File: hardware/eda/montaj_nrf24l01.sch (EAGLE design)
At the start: 4 parts, among them X1 MINI-USB-SHIELD-UX60-MB-5S8

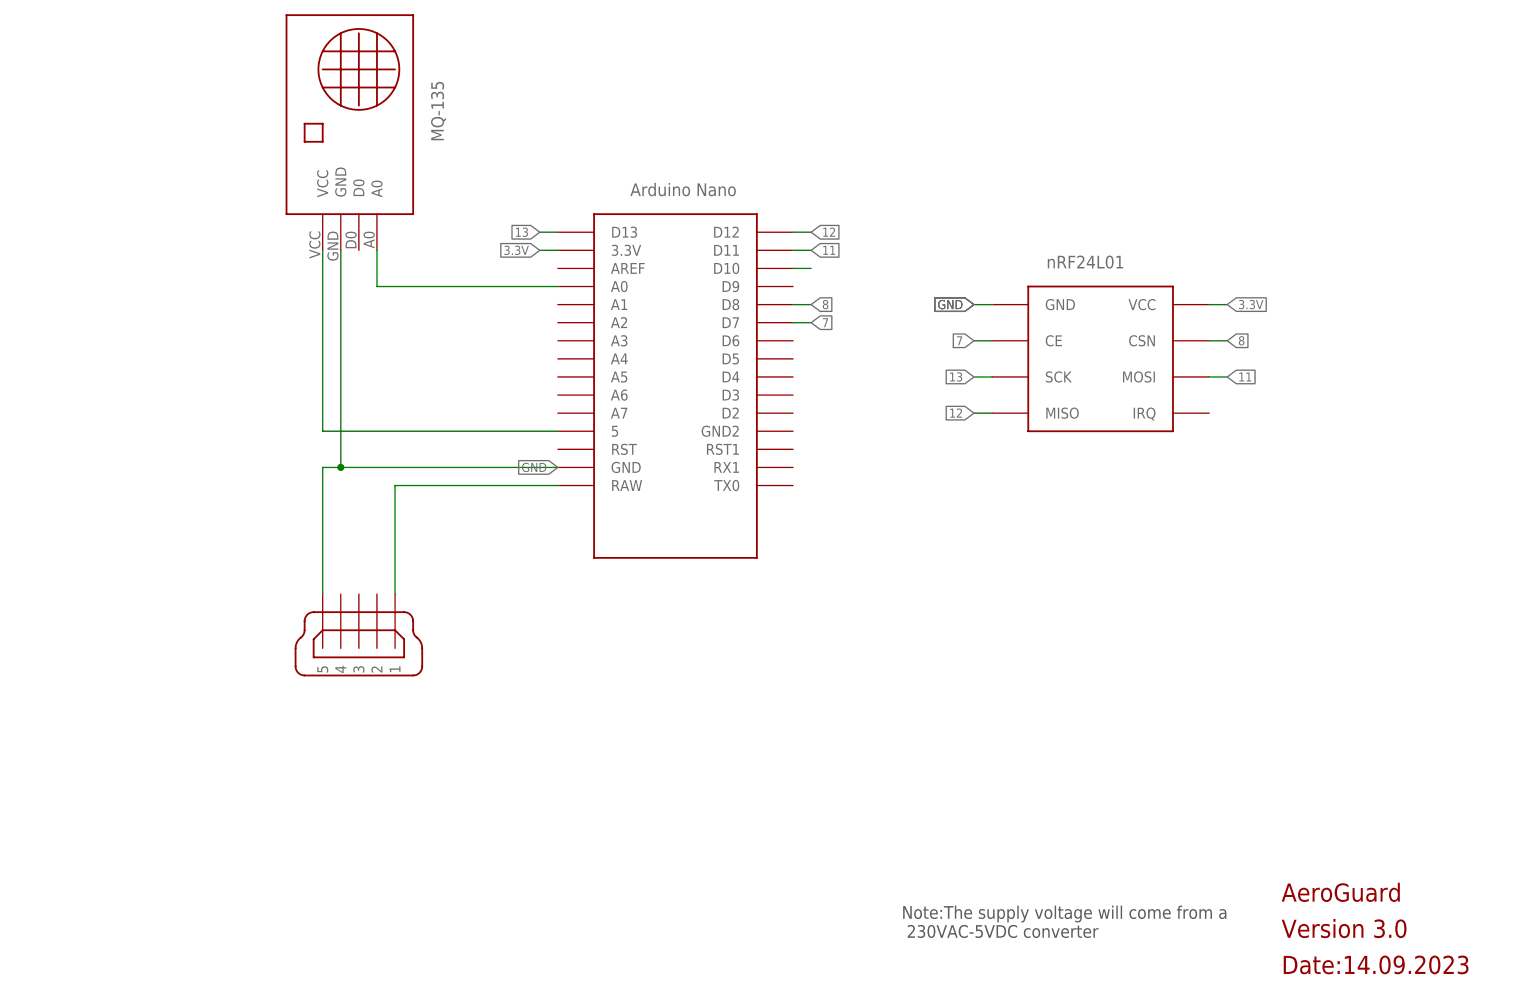
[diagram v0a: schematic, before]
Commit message: Adaugare modul DHT11
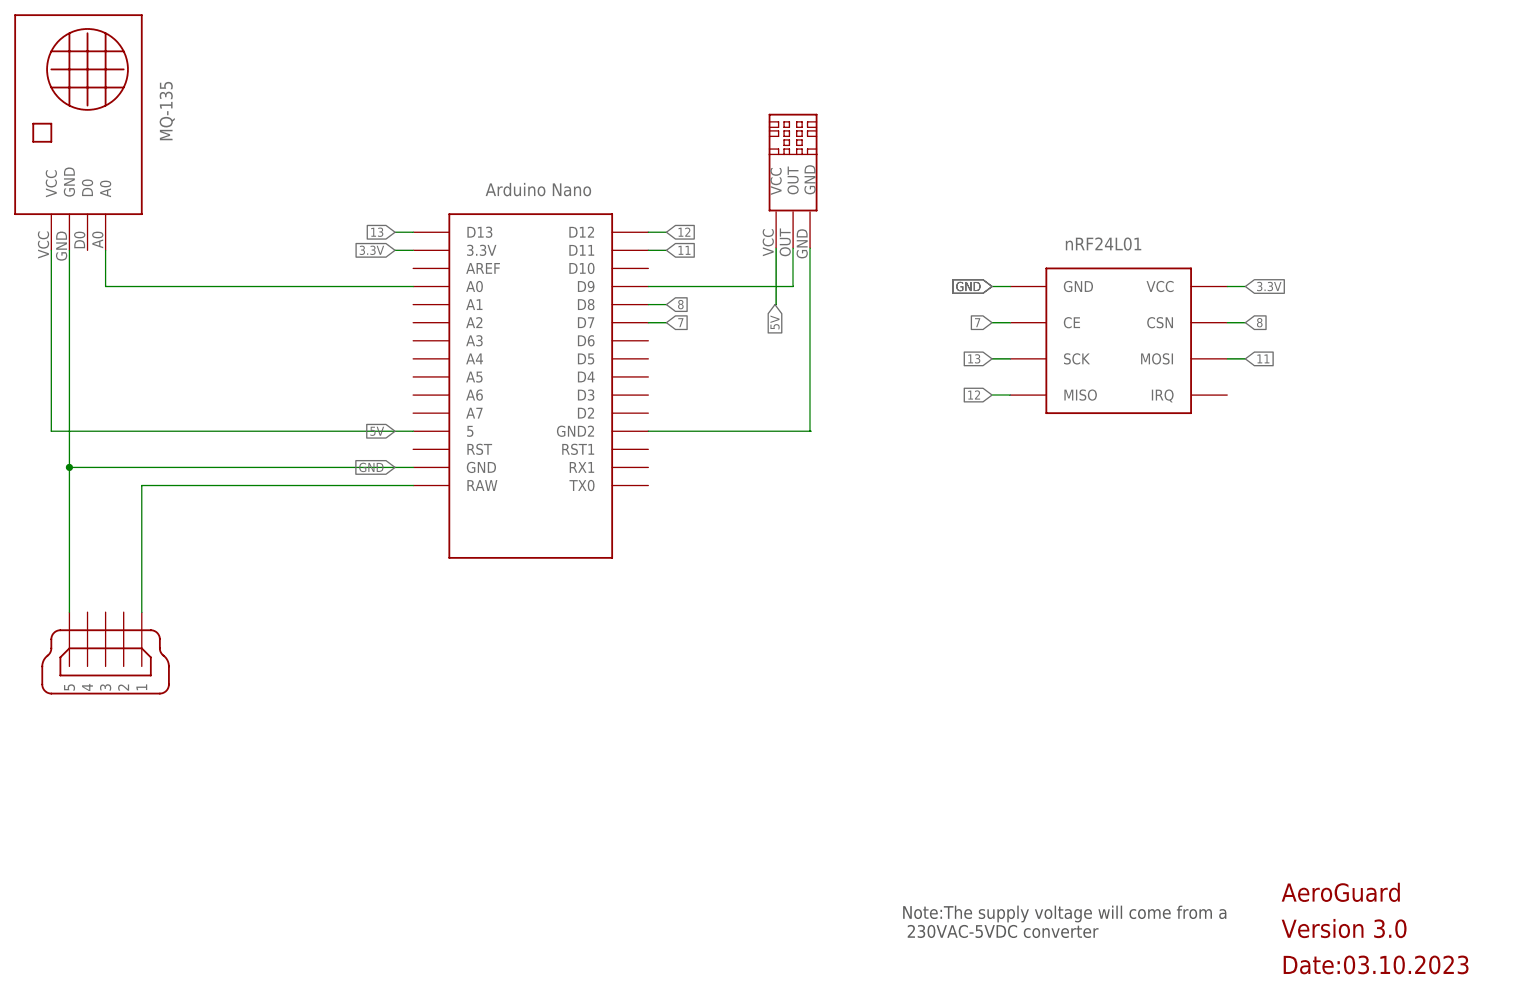
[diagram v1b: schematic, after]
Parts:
- added U$1: DHT11, componente:DHT11
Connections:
- net N$3 renamed 5V
- new net N$11: GND.GND2, U$1.GND
- new net N$3: GND.D9, U$1.OUT
- net N$6: now also U$1.VCC; no longer GND.D10
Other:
- note added: "Date:03.10.2023"
- note removed: "Date:14.09.2023"
